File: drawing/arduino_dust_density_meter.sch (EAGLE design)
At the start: 7 parts

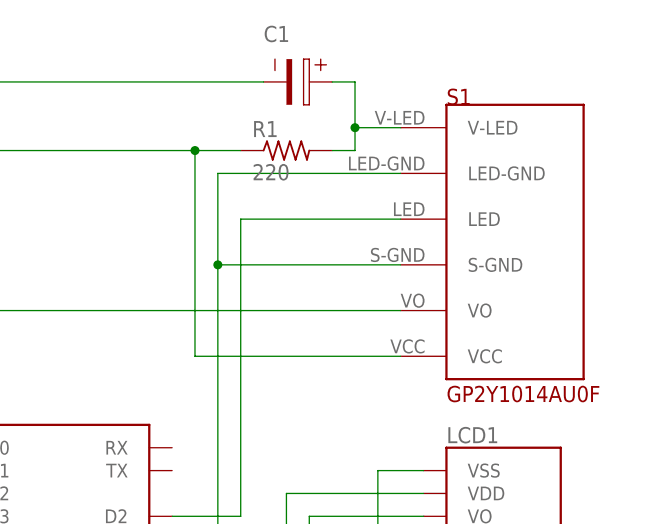
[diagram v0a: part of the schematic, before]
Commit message: [REFACTOR] Change sensor library
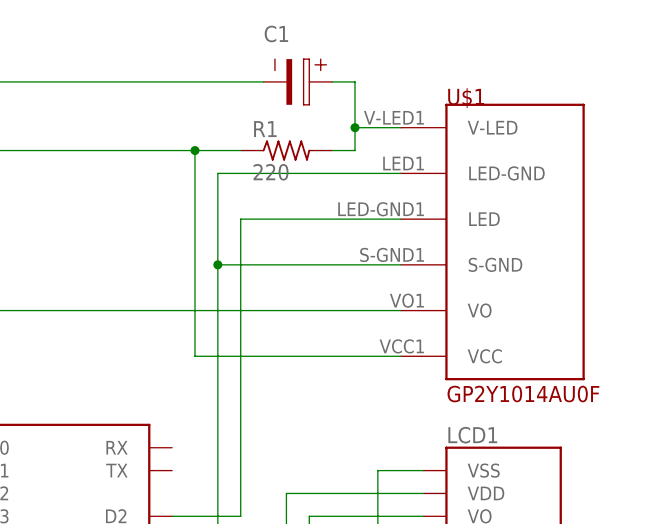
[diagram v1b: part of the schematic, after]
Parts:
- removed S1: GP2Y1014AU0F, sharp-dust-sensor:GP2Y1014AU0F
- added U$1: GP2Y1014AU0F, sharp-dust-sensor:GP2Y1014AU0F
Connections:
- net N$1: now also U$1.V-LED; no longer S1.V-LED
- net N$2: now also U$1.VCC; no longer S1.VCC
- net N$4: now also U$1.LED-GND, U$1.S-GND; no longer S1.LED-GND, S1.S-GND
- net N$5: now also U$1.LED; no longer S1.LED
- net N$6: now also U$1.VO; no longer S1.VO
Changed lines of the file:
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@@
 <parts>
 <part name="B1" library="SparkFun-Boards" library_urn="urn:adsk.eagle:library:509" deviceset="ARDUINO_UNO_R3_SHIELD" device="BASIC" package3d_urn="urn:adsk.eagle:package:37321/1" value="ARDUINO_UNO_R3"/>
-<part name="S1" library="sharp-dust-sensor" library_urn="urn:adsk.eagle:library:12467232" deviceset="GP2Y1014AU0F" device="" package3d_urn="urn:adsk.eagle:package:12467238/4"/>
 <part name="R1" library="BeagleBone_Black_Wireless" library_urn="urn:adsk.eagle:library:6644236" deviceset="R-US_" device="0309/12" package3d_urn="urn:adsk.eagle:package:8118473/1" value="220"/>
 <part name="C1" library="Wurth_Elektronik_Passive_Capacitors_rev18b" library_urn="urn:adsk.eagle:library:491551" deviceset="WCAP-PTG5" device="_870025575007" package3d_urn="urn:adsk.eagle:package:491745/2" technology="_10X12,5"/>
@@
 <part name="R2" library="BeagleBone_Black_Wireless" library_urn="urn:adsk.eagle:library:6644236" deviceset="R-US_" device="0309/12" package3d_urn="urn:adsk.eagle:package:8118473/1" value="1k"/>
 <part name="R3" library="BeagleBone_Black_Wireless" library_urn="urn:adsk.eagle:library:6644236" deviceset="R-US_" device="0309/12" package3d_urn="urn:adsk.eagle:package:8118473/1" value="1k"/>
+<part name="U$1" library="sharp-dust-sensor" library_urn="urn:adsk.eagle:library:12467483" deviceset="GP2Y1014AU0F" device="" package3d_urn="urn:adsk.eagle:package:12467238/6"/>
 </parts>
 <sheets>
@@
 <attribute name="NAME" x="104.648" y="58.674" size="1.778" layer="95" font="vector"/>
 <attribute name="VALUE" x="105.41" y="12.446" size="1.778" layer="96" font="vector" align="top-left"/>
-</instance>
-<instance part="S1" gate="G$1" x="165.1" y="78.74" smashed="yes">
-<attribute name="NAME" x="157.48" y="93.98" size="1.778" layer="94"/>
-<attribute name="VALUE" x="157.48" y="60.96" size="1.778" layer="94"/>
 </instance>
 <instance part="R1" gate="G$1" x="139.7" y="88.9" smashed="yes">
@@
 <attribute name="VALUE" x="145.542" y="3.81" size="1.778" layer="96" rot="R90"/>
 </instance>
+<instance part="U$1" gate="&gt;NAME" x="165.1" y="78.74" smashed="yes">
+<attribute name="NAME" x="157.48" y="93.98" size="1.778" layer="94"/>
+<attribute name="VALUE" x="157.48" y="60.96" size="1.778" layer="94"/>
+</instance>
 </instances>
 <busses>
@@
 <net name="N$1" class="0">
 <segment>
-<pinref part="S1" gate="G$1" pin="V-LED"/>
 <wire x1="152.4" y1="91.44" x2="147.32" y2="91.44" width="0.1524" layer="91"/>
 <pinref part="C1" gate="G$1" pin="1"/>
@@
 <wire x1="147.32" y1="88.9" x2="147.32" y2="91.44" width="0.1524" layer="91"/>
 <junction x="147.32" y="91.44"/>
+<pinref part="U$1" gate="&gt;NAME" pin="V-LED"/>
 </segment>
 </net>
@@
 <wire x1="99.06" y1="7.62" x2="132.08" y2="7.62" width="0.1524" layer="91"/>
 <wire x1="132.08" y1="7.62" x2="132.08" y2="15.24" width="0.1524" layer="91"/>
-<pinref part="S1" gate="G$1" pin="LED-GND"/>
 <wire x1="132.08" y1="15.24" x2="132.08" y2="76.2" width="0.1524" layer="91"/>
 <wire x1="132.08" y1="76.2" x2="132.08" y2="86.36" width="0.1524" layer="91"/>
 <wire x1="132.08" y1="86.36" x2="152.4" y2="86.36" width="0.1524" layer="91"/>
-<pinref part="S1" gate="G$1" pin="S-GND"/>
 <wire x1="152.4" y1="76.2" x2="132.08" y2="76.2" width="0.1524" layer="91"/>
 <junction x="132.08" y="76.2"/>
@@
 <wire x1="147.32" y1="12.7" x2="147.32" y2="15.24" width="0.1524" layer="91"/>
 <junction x="147.32" y="15.24"/>
+<pinref part="U$1" gate="&gt;NAME" pin="LED-GND"/>
+<pinref part="U$1" gate="&gt;NAME" pin="S-GND"/>
 </segment>
 </net>
 <net name="N$5" class="0">
 <segment>
-<pinref part="S1" gate="G$1" pin="LED"/>
 <wire x1="152.4" y1="81.28" x2="134.62" y2="81.28" width="0.1524" layer="91"/>
 <wire x1="134.62" y1="81.28" x2="134.62" y2="48.26" width="0.1524" layer="91"/>
 <pinref part="B1" gate="G$1" pin="D2"/>
 <wire x1="134.62" y1="48.26" x2="127" y2="48.26" width="0.1524" layer="91"/>
+<pinref part="U$1" gate="&gt;NAME" pin="LED"/>
 </segment>
 </net>
 <net name="N$6" class="0">
 <segment>
-<pinref part="S1" gate="G$1" pin="VO"/>
 <wire x1="152.4" y1="71.12" x2="99.06" y2="71.12" width="0.1524" layer="91"/>
 <wire x1="99.06" y1="71.12" x2="99.06" y2="55.88" width="0.1524" layer="91"/>
 <pinref part="B1" gate="G$1" pin="A0"/>
 <wire x1="99.06" y1="55.88" x2="101.6" y2="55.88" width="0.1524" layer="91"/>
+<pinref part="U$1" gate="&gt;NAME" pin="VO"/>
 </segment>
 </net>
 <net name="N$2" class="0">
 <segment>
-<pinref part="S1" gate="G$1" pin="VCC"/>
 <wire x1="152.4" y1="66.04" x2="129.54" y2="66.04" width="0.1524" layer="91"/>
 <pinref part="R1" gate="G$1" pin="1"/>
@@
 <wire x1="139.7" y1="50.8" x2="139.7" y2="-2.54" width="0.1524" layer="91"/>
 <junction x="139.7" y="-2.54"/>
+<pinref part="U$1" gate="&gt;NAME" pin="VCC"/>
 </segment>
 </net>
